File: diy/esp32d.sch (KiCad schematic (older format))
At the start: 47 parts, among them IC1 CP2102N-A01-GQFN28R, J1 Conn_02x08_Odd_Even, J2 Conn_02x08_Odd_Even, J4 Conn_01x02, Q1 SS8050-G, Q2 SS8050-G, Q3 DMG2307L-7, SW1 SW_Push, U1 AMS1117-3.3, U2 ESP32-WROOM-32D, U3 DizzyBITLogo, U4 MCP73831-2-OT, U5 DizzyBIT-Layout

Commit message: Changed blue led PN for 3.3V
Added DIY project folder
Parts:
- R3, R4: footprint Resistor_SMD:R_0603_1608Metric -> Resistor_THT:R_Axial_DIN0204_L3.6mm_D1.6mm_P7.62mm_Horizontal; dk_pn 311-4.7KGRTR-ND -> (none); dk_web https://www.digikey.com/product-detail/en/yageo/RC0603JR-07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 -> (none); pn RC0603JR-074K7L -> (none)
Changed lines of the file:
@@
 EESchema Schematic File Version 4
-LIBS:esp32d-cache
 EELAYER 26 0
 EELAYER END
@@
 F 0 "R3" V 5150 3800 50  0000 L CNN
 F 1 "R4.7K" V 5150 3975 50  0000 L CNN
-F 2 "Resistor_SMD:R_0603_1608Metric" V 5180 4150 50  0001 C CNN
+F 2 "Resistor_THT:R_Axial_DIN0204_L3.6mm_D1.6mm_P7.62mm_Horizontal" V 5180 4150 50  0001 C CNN
 F 3 "" H 5250 4150 50  0001 C CNN
-F 4 "311-4.7KGRTR-ND" H 5250 4150 50  0001 C CNN "dk_pn"
-F 5 "RC0603JR-074K7L" H 5250 4150 50  0001 C CNN "pn"
-F 6 "https://www.digikey.com/product-detail/en/yageo/RC0603JR-074K7L/311-4.7KGRTR-ND/726785" H 5250 4150 50  0001 C CNN "dk_web"
 	1    5250 4150
 	-1   0    0    1
@@
 Wire Wire Line
 	5250 4300 6175 4300
-Wire Wire Line
-	3775 4400 5625 4400
-$Comp
-L Device:R R4
-U 1 1 5C9418C5
-P 5625 4250
-F 0 "R4" V 5525 3900 50  0000 L CNN
-F 1 "R4.7K" V 5525 4075 50  0000 L CNN
-F 2 "Resistor_SMD:R_0603_1608Metric" V 5555 4250 50  0001 C CNN
-F 3 "" H 5625 4250 50  0001 C CNN
-F 4 "311-4.7KGRTR-ND" H 5625 4250 50  0001 C CNN "dk_pn"
-F 5 "RC0603JR-074K7L" H 5625 4250 50  0001 C CNN "pn"
-F 6 "https://www.digikey.com/product-detail/en/yageo/RC0603JR-074K7L/311-4.7KGRTR-ND/726785" H 5625 4250 50  0001 C CNN "dk_web"
-	1    5625 4250
-	-1   0    0    1
-$EndComp
-Connection ~ 5625 4400
-Wire Wire Line
-	5625 4400 6175 4400
 Wire Wire Line
 	5250 4000 5250 1850
@@
 	1    0    0    -1
 $EndComp
+Wire Wire Line
+	3775 4400 5625 4400
+$Comp
+L Device:R R4
+U 1 1 5D9ADC4E
+P 5625 4250
+F 0 "R4" V 5525 3900 50  0000 L CNN
+F 1 "R4.7K" V 5525 4075 50  0000 L CNN
+F 2 "Resistor_THT:R_Axial_DIN0204_L3.6mm_D1.6mm_P7.62mm_Horizontal" V 5555 4250 50  0001 C CNN
+F 3 "" H 5625 4250 50  0001 C CNN
+	1    5625 4250
+	-1   0    0    1
+$EndComp
+Connection ~ 5625 4400
+Wire Wire Line
+	5625 4400 6175 4400
 $EndSCHEMATC

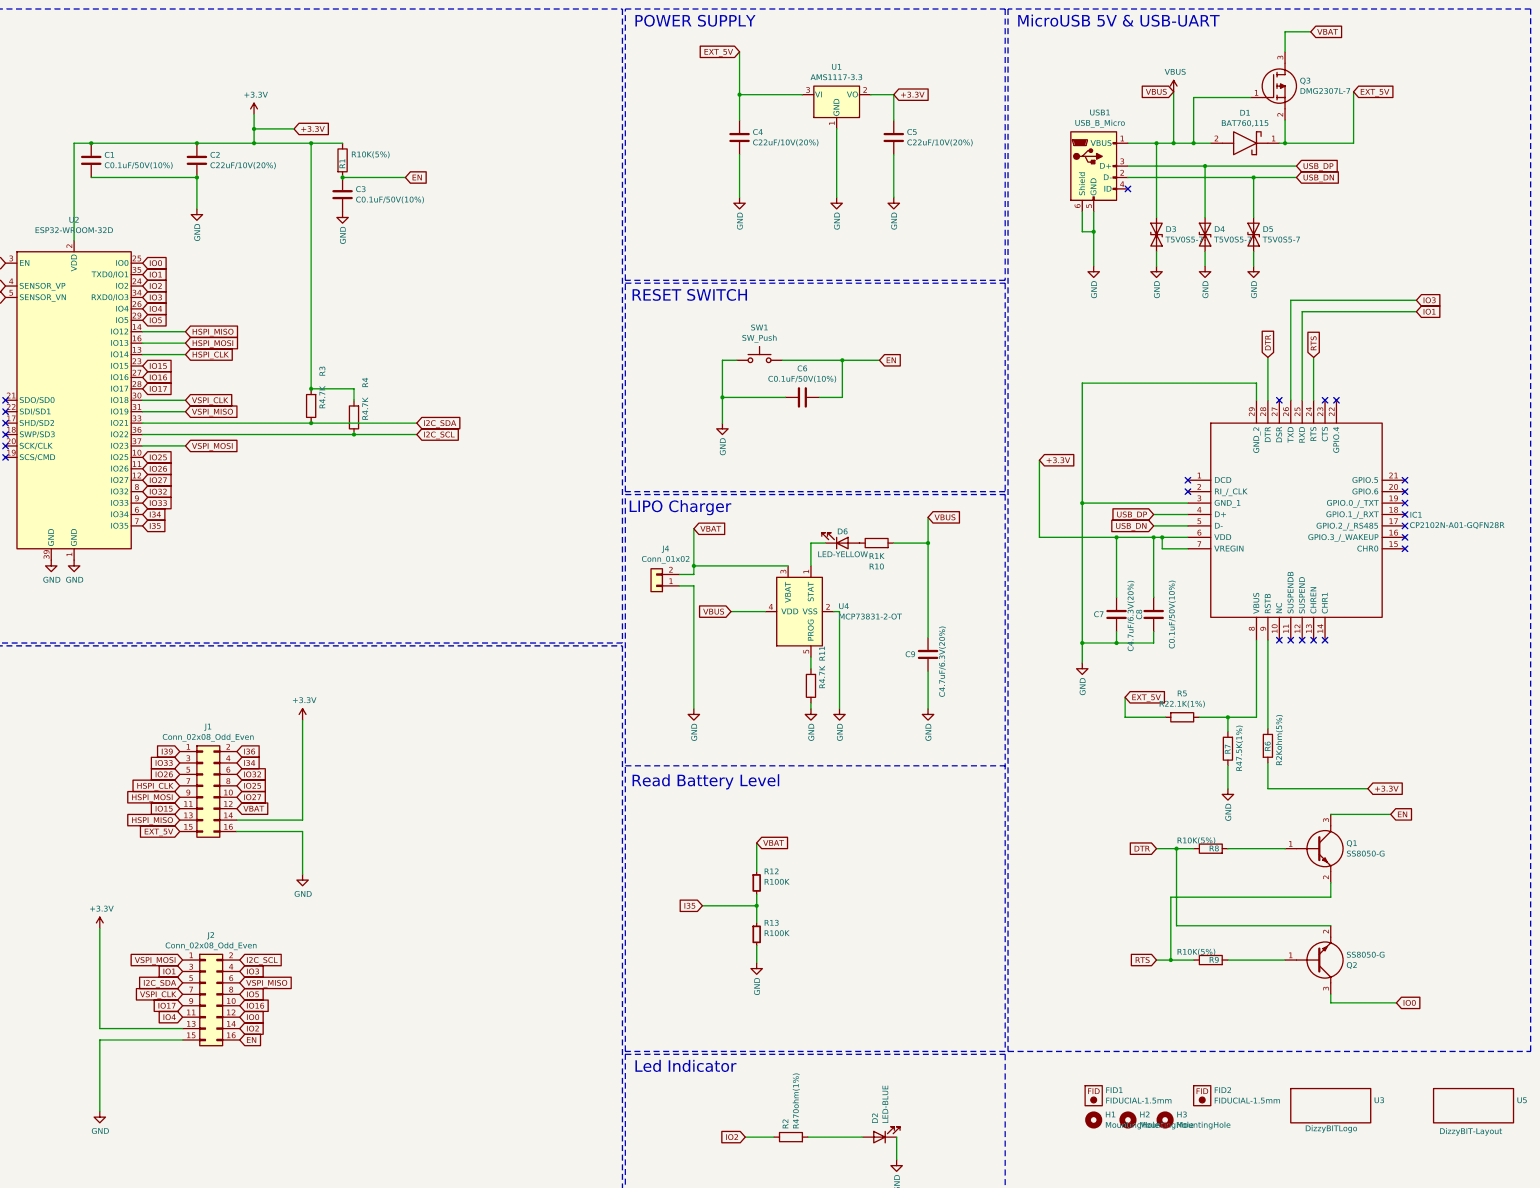
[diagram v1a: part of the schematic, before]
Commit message: Added DIY board
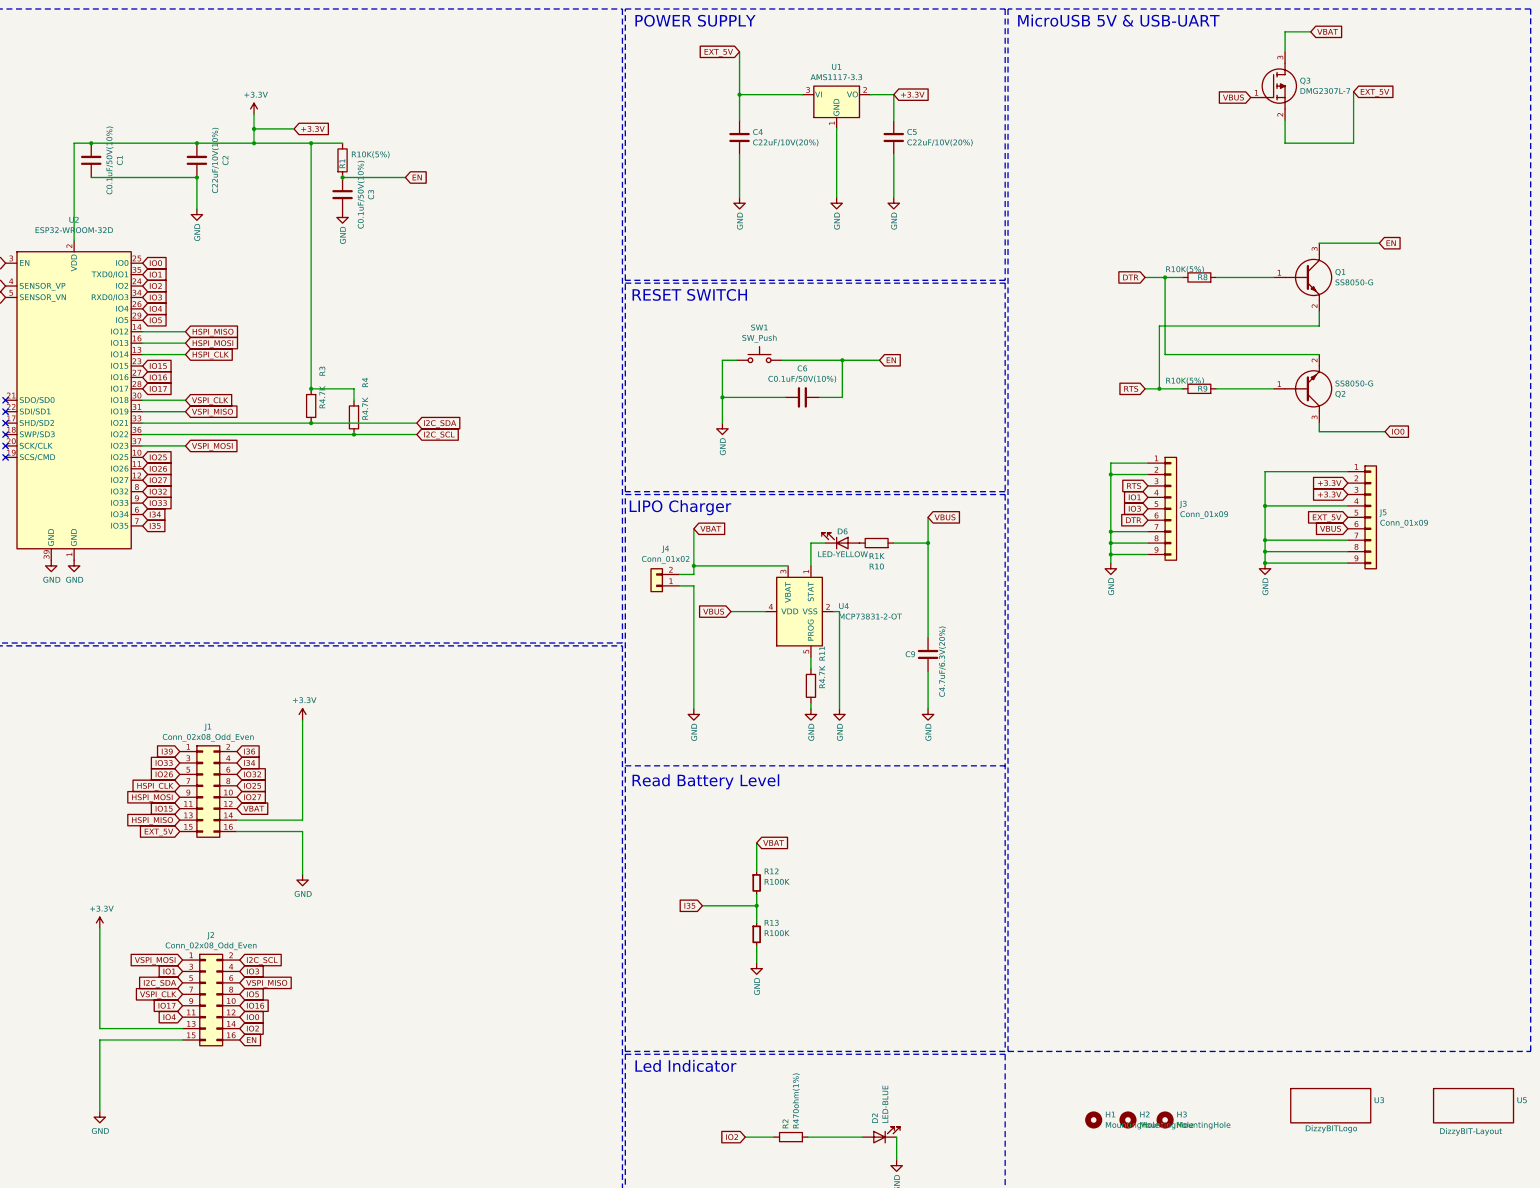
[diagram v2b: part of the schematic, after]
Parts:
- removed C7: C4.7uF/6.3V(20%), Capacitor_SMD:C_0603_1608Metric, symbol Device:C
- removed C8: C0.1uF/50V(10%), Capacitor_SMD:C_0603_1608Metric, symbol Device:C
- removed D1: BAT760,115, SOD2513X120N, symbol SamacSys_Parts:BAT760-7
- removed D3, D4, D5: T5V0S5-7, smd-semi:SOD-523, symbol Device:D_TVS
- removed FID1, FID2: FIDUCIAL-1.5mm, fab:FIDUCIAL-1.5mm, symbol pcb:FIDUCIAL-1.5mm
- removed IC1: CP2102N-A01-GQFN28R, SamacSys_Parts:QFN50P500X500X80-29N-D, symbol SamacSys_Parts:CP2102N-A01-GQFN28R
- removed R5: R22.1K(1%), Capacitor_SMD:C_0603_1608Metric, symbol Device:R
- removed R6: R2Kohm(5%), Resistor_SMD:R_0603_1608Metric, symbol Device:R
- removed R7: R47.5K(1%), Capacitor_SMD:C_0603_1608Metric, symbol Device:R
- removed USB1: USB_B_Micro, Connfly:DS1105-12, symbol Connector:USB_B_Micro
- added J3, J5: Conn_01x09, symbol Connector_Generic:Conn_01x09
- C1, C3, C6: footprint Capacitor_SMD:C_0603_1608Metric -> Capacitor_THT:C_Disc_D3.8mm_W2.6mm_P2.50mm; dk_pn 311-1366-6-ND -> (none); pn CC0603MRY5V9BB104 -> K104K15X7RF5TL2
- C2: value C22uF/10V(20%) -> C22uF/10V(10%); footprint Capacitor_SMD:C_0603_1608Metric -> Capacitor_THT:C_Disc_D3.8mm_W2.6mm_P2.50mm; dk_pn 490-10476-2-ND -> (none); pn GRM188R61A226ME15D -> K104K15X7RF5TL2
- D2: footprint LED_SMD:LED_0805_2012Metric -> LED_THT:LED_D3.0mm; dk_pn FC-A2012BK-470H2 -> 1497-1003-ND; pn FC-A2012BK-470H2 -> XLFBB11W
- D6: footprint LED_SMD:LED_0805_2012Metric -> LED_THT:LED_D3.0mm; dk_pn 475-2560-1-ND -> (none); dk_web https://www.digikey.com/product-detail/en/osram-opto-semico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 -> (none); pn LY R976-PS-36 -> (none)
- R1: footprint Resistor_SMD:R_0603_1608Metric -> Resistor_THT:R_Axial_DIN0204_L3.6mm_D1.6mm_P7.62mm_Horizontal; dk_pn RHM10KDTR-ND -> (none); pn ESR03EZPJ103 -> (none)
- R10: footprint Resistor_SMD:R_0805_2012Metric -> Resistor_THT:R_Axial_DIN0204_L3.6mm_D1.6mm_P7.62mm_Horizontal; pn 0805W8F1001T5E -> (none)
- R12, R13: footprint Resistor_SMD:R_0603_1608Metric -> Resistor_THT:R_Axial_DIN0204_L3.6mm_D1.6mm_P7.62mm_Horizontal; dk_pn RR08P100KDTR-ND -> (none); dk_web https://www.digikey.com/product-detail/en/susumu/RR0816P-10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 -> (none); pn RR0816P-104-D -> (none)
- R2: footprint Resistor_SMD:R_0603_1608Metric -> Resistor_THT:R_Axial_DIN0204_L3.6mm_D1.6mm_P7.62mm_Horizontal; dk_pn 311-470HRTR-ND -> (none); pn RC0603FR-07470RL -> (none)
- SW1: footprint Button_Switch_SMD:TL3340 -> SamacSys_Parts:TL3340; dk_pn EG4627TR-ND -> (none); pn TL3340AF160QG -> (none)
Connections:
- net +3V3: now also C1.1, J5.2 (Pin_2), J5.3 (Pin_3); no longer C1.2
- net DTR: now also J3.6 (Pin_6)
- net EN: now also C3.1; no longer C3.2
- net EXT_5V: now also J5.5 (Pin_5)
- net GND: now also C1.2, C3.2, J3.1 (Pin_1), J3.2 (Pin_2), J3.7 (Pin_7), J3.8 (Pin_8), J3.9 (Pin_9), J5.1 (Pin_1), J5.4 (Pin_4), J5.7 (Pin_7), J5.8 (Pin_8), J5.9 (Pin_9); no longer C1.1, C3.1
- net IO1: now also J3.4 (Pin_4)
- net IO3: now also J3.5 (Pin_5)
- net RTS: now also J3.3 (Pin_3)
- net VBUS: now also J5.6 (Pin_6)
- no-connect marks 24 -> 6
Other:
- moved on the sheet: Q1, Q2, R8, R9

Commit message: Finished the DIY board
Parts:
- removed J3, J5: Conn_01x09, symbol Connector_Generic:Conn_01x09
- added H4: MountingHole_Pad, MountingHole:MountingHole_2.2mm_M2_DIN965_Pad, symbol Mechanical:MountingHole_Pad
- added U6: DizzyBit-MicroUSB-UART, DizzyBit:DizzyBit-MicroUSB-UART, symbol Altera:DizzyBit-MicroUSB-UART
- C2: pn K104K15X7RF5TL2 -> (none)
- C4, C5: value C22uF/10V(20%) -> C22uF/10V(10%); footprint Capacitor_SMD:C_0603_1608Metric -> Capacitor_THT:C_Disc_D3.8mm_W2.6mm_P2.50mm; dk_pn 490-10476-2-ND -> (none); pn GRM188R61A226ME15D -> (none)
- C9: footprint Capacitor_SMD:C_0603_1608Metric -> Capacitor_THT:C_Disc_D3.8mm_W2.6mm_P2.50mm; dk_pn 1276-1907-2-ND -> (none); pn CL10A475MQ8NNNC -> (none)
- J4: footprint Connector_JST:JST_PH_S2B-PH-SM4-TB_1x02-1MP_P2.00mm_Horizontal -> Connector_JST:JST_PH_S2B-PH-K_1x02_P2.00mm_Horizontal; pn DS1066-06-2-M-R-B-1-R -> (none)
- Q1, Q2: value SS8050-G -> SS8050DTA; footprint digikey-footprints:SOT-23-3 -> Package_TO_SOT_THT:TO-92_Inline_Wide; Manufacturer_Name Comchip Technology -> (none); Mouser Part Number 750-SS8050-G -> (none); dk_pn 641-1790-2-ND -> SS8050DTACT-ND; pn SS8050-G -> SS8050DTA
- Q3: footprint Package_TO_SOT_SMD:SOT-23 -> Package_TO_SOT_SMD:SOT-23W_Handsoldering; dk_pn DMG2307L-7DITR-ND -> (none); dk_web https://www.digikey.com/product-detail/en/diodes-incorporat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 -> (none); pn DMG2307L-7 -> (none)
- R11: footprint Resistor_SMD:R_0603_1608Metric -> Resistor_THT:R_Axial_DIN0204_L3.6mm_D1.6mm_P7.62mm_Horizontal; dk_pn 311-4.7KGRTR-ND -> (none); dk_web https://www.digikey.com/product-detail/en/yageo/RC0603JR-07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 -> (none); pn RC0603JR-074K7L -> (none)
- R8, R9: footprint Resistor_SMD:R_0603_1608Metric -> Resistor_THT:R_Axial_DIN0204_L3.6mm_D1.6mm_P7.62mm_Horizontal; dk_pn RHM10KDTR-ND -> (none); pn ESR03EZPJ103 -> (none)
- SW1: footprint SamacSys_Parts:TL3340 -> Button_Switch_SMD:TL3340-HandSoldering
- U1: footprint Package_TO_SOT_SMD:SOT-223-3_TabPin2 -> Package_TO_SOT_SMD:SOT-223-3_TabPin2-HandSoldering
- U4: footprint Package_TO_SOT_SMD:SOT-23-5 -> Package_TO_SOT_SMD:SOT-23-5_HandSoldering
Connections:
- net +3V3: now also U6.13 (+3.3v), U6.14 (+3.3v)
- net DTR: now also Q2.3, U6.6 (GND); no longer Q2.2
- net EXT_5V: now also U6.15 (EXT_5V)
- net GND: now also H4.1, U6.1 (GND), U6.10 (GND), U6.11 (GND), U6.12 (GND), U6.17 (GND), U6.18 (GND), U6.2 (GND), U6.7 (GND), U6.8 (GND), U6.9 (GND)
- net IO0: now also Q2.2; no longer Q2.3
- net IO1: now also U6.4 (RXD)
- net IO3: now also U6.5 (DTR)
- net RTS: now also U6.3 (RTS)
- net VBUS: now also U6.16 (VBUS)
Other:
- moved on the sheet: H1, H2, H3
